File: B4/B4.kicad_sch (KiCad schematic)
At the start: 0 parts

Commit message: B0 ready for v0.2.0 release.
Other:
- sheet buses ports: added DZ[0..7], D[0..7], ~{EN[0..15]}; removed {DATABUS}, {ENABLEBUS}
- company: (none) -> Daniel Molina
- title: (none) -> 74HCT6526 Board 4
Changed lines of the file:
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@@
 (kicad_sch (version 20211123) (generator eeschema)
   (paper "A4")
+  (title_block
+    (title "74HCT6526 Board 4")
+    (date "2023-01-22")
+    (rev "0.2.0")
+    (company "Daniel Molina")
+    (comment 1 "https://github.com/dmolinagarcia/74HCT6526")
+  )
   (bus_alias "ENABLEBUS" (members "~{EN[0..15]}"))
   (bus_alias "DATABUS" (members "D[0..7]" "DZ[0..7]"))
@@
   (junction (at 43.18 17.78) (diameter 1.016) (color 0 0 0 0)
   )
-  (junction (at 48.26 22.86) (diameter 0.9144) (color 0 0 0 0)
+  (junction (at 48.26 25.4) (diameter 0) (color 0 0 0 0)
+  )
+  (junction (at 50.8 22.86) (diameter 0) (color 0 0 0 0)
   )
   (junction (at 45.72 20.32) (diameter 1.016) (color 0 0 0 0)
@@
     (stroke (width 0) (type solid) (color 0 0 0 0))
   )
+  (bus (pts (xy 48.26 50.8) (xy 48.26 25.4))
+    (stroke (width 0) (type default) (color 0 0 0 0))
+  )
   (bus (pts (xy 43.18 17.78) (xy 284.48 17.78))
     (stroke (width 0) (type solid) (color 0 0 0 0))
   )
-  (bus (pts (xy 40.64 50.8) (xy 48.26 50.8))
+  (bus (pts (xy 40.64 53.34) (xy 50.8 53.34))
     (stroke (width 0) (type solid) (color 0 0 0 0))
   )
@@
     (stroke (width 0) (type solid) (color 0 0 0 0))
   )
-  (bus (pts (xy 48.26 50.8) (xy 48.26 22.86))
+  (bus (pts (xy 50.8 53.34) (xy 50.8 22.86))
     (stroke (width 0) (type solid) (color 0 0 0 0))
   )
   (bus (pts (xy 40.64 45.72) (xy 43.18 45.72))
     (stroke (width 0) (type solid) (color 0 0 0 0))
+  )
+  (bus (pts (xy 48.26 25.4) (xy 284.48 25.4))
+    (stroke (width 0) (type default) (color 0 0 0 0))
+  )
+  (bus (pts (xy 40.64 25.4) (xy 48.26 25.4))
+    (stroke (width 0) (type default) (color 0 0 0 0))
+  )
+  (bus (pts (xy 40.64 50.8) (xy 48.26 50.8))
+    (stroke (width 0) (type default) (color 0 0 0 0))
   )
   (bus (pts (xy 43.18 17.78) (xy 43.18 45.72))
@@
     (stroke (width 0) (type solid) (color 0 0 0 0))
   )
-  (bus (pts (xy 40.64 22.86) (xy 48.26 22.86))
+  (bus (pts (xy 40.64 22.86) (xy 50.8 22.86))
     (stroke (width 0) (type solid) (color 0 0 0 0))
   )
-  (bus (pts (xy 48.26 22.86) (xy 284.48 22.86))
+  (bus (pts (xy 50.8 22.86) (xy 284.48 22.86))
     (stroke (width 0) (type solid) (color 0 0 0 0))
   )
@@
     (stroke (width 0) (type solid) (color 0 0 0 0))
   )
-  (label "{DATABUS}" (at 281.94 20.32 180)
-    (effects (font (size 1.27 1.27)) (justify right bottom))
-  )
-  (label "{ENABLEBUS}" (at 281.94 22.86 180)
-    (effects (font (size 1.27 1.27)) (justify right bottom))
-  )
   (label "{CONTROLBUS}" (at 281.94 17.78 180)
     (effects (font (size 1.27 1.27)) (justify right bottom))
   )
-  (global_label "{DATABUS}" (shape input) (at 40.64 20.32 180)
+  (global_label "D[0..7]" (shape input) (at 40.64 20.32 180)
     (effects (font (size 1.27 1.27)) (justify right))
     (property "Intersheet References" "${INTERSHEET_REFS}" (id 0) (at 26.7848 20.2406 0)
@@
     )
   )
-  (global_label "{ENABLEBUS}" (shape input) (at 40.64 22.86 180)
+  (global_label "~{EN[0..15]}" (shape input) (at 40.64 22.86 180)
     (effects (font (size 1.27 1.27)) (justify right))
     (property "Intersheet References" "${INTERSHEET_REFS}" (id 0) (at 24.1843 22.7806 0)
@@
     (effects (font (size 1.27 1.27)) (justify right))
     (property "Intersheet References" "${INTERSHEET_REFS}" (id 0) (at 22.6724 17.7006 0)
+      (effects (font (size 1.27 1.27)) (justify right) hide)
+    )
+  )
+  (global_label "DZ[0..7]" (shape input) (at 40.64 25.4 180)
+    (effects (font (size 1.27 1.27)) (justify right))
+    (property "Intersheet References" "${INTERSHEET_REFS}" (id 0) (at 26.7848 25.3206 0)
       (effects (font (size 1.27 1.27)) (justify right) hide)
     )
@@
       (effects (font (size 1.27 1.27)) (justify right))
     )
-    (pin "{DATABUS}" bidirectional (at 40.64 48.26 0)
+    (pin "D[0..7]" bidirectional (at 40.64 48.26 0)
       (effects (font (size 1.27 1.27)) (justify right))
     )
-    (pin "{ENABLEBUS}" input (at 40.64 50.8 0)
+    (pin "~{EN[0..15]}" input (at 40.64 53.34 0)
+      (effects (font (size 1.27 1.27)) (justify right))
+    )
+    (pin "DZ[0..7]" bidirectional (at 40.64 50.8 0)
       (effects (font (size 1.27 1.27)) (justify right))
     )
@@
       (reference "#PWR04") (unit 1) (value "GND") (footprint "")
     )
+    (path "/ab70af84-b545-4f99-8702-a579edb051a6/8554bcb8-444f-4ed6-8d2e-98ad945f68d5"
+      (reference "#PWR?") (unit 1) (value "GND") (footprint "")
+    )
+    (path "/ab70af84-b545-4f99-8702-a579edb051a6/989f85db-f560-481a-baba-d8c4193b2250"
+      (reference "C400") (unit 1) (value "100n") (footprint "")
+    )
     (path "/ab70af84-b545-4f99-8702-a579edb051a6/eb77a2b8-05ae-49a3-b81c-407677587e70"

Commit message: Ready for v0.2.1
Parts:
- added U401, U402: 74HC00, symbol 74xx:74HC00
- added U403: 74HC04, Package_SO:SOIC-14_3.9x8.7mm_P1.27mm, symbol 74xx:74HC04
- added U404, U405, U406: 74HC32, symbol 74xx:74LS32
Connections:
- new net PHI2: U403.1
- new net ~{PHI2}: U403.2
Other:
- added sheet todAlarm (todAlarm.kicad_sch)
- added sheet todComparator (todComparator.kicad_sch)
- added sheet todControl (todControl.kicad_sch)
- added sheet todCounter (todCounter.kicad_sch)
- added sheet todOutput (todOutput.kicad_sch)

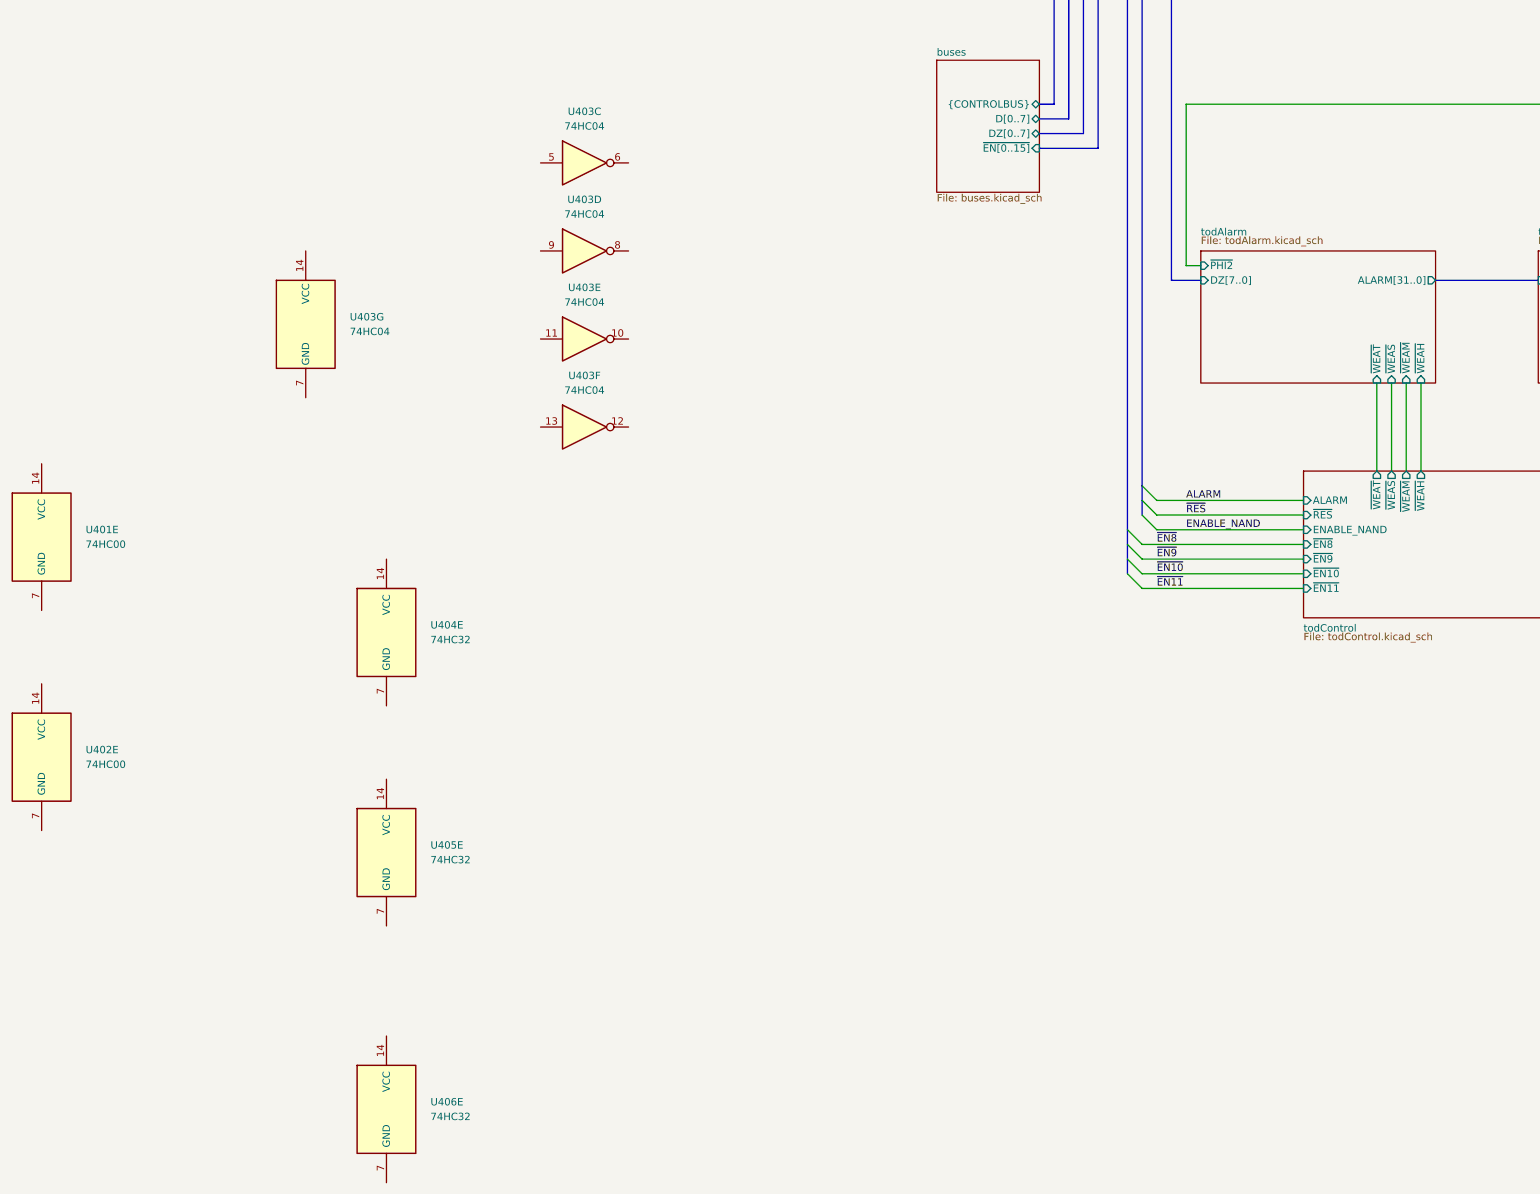
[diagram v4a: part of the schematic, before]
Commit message: B2 refactored. B4 Added. TOD sch completed.
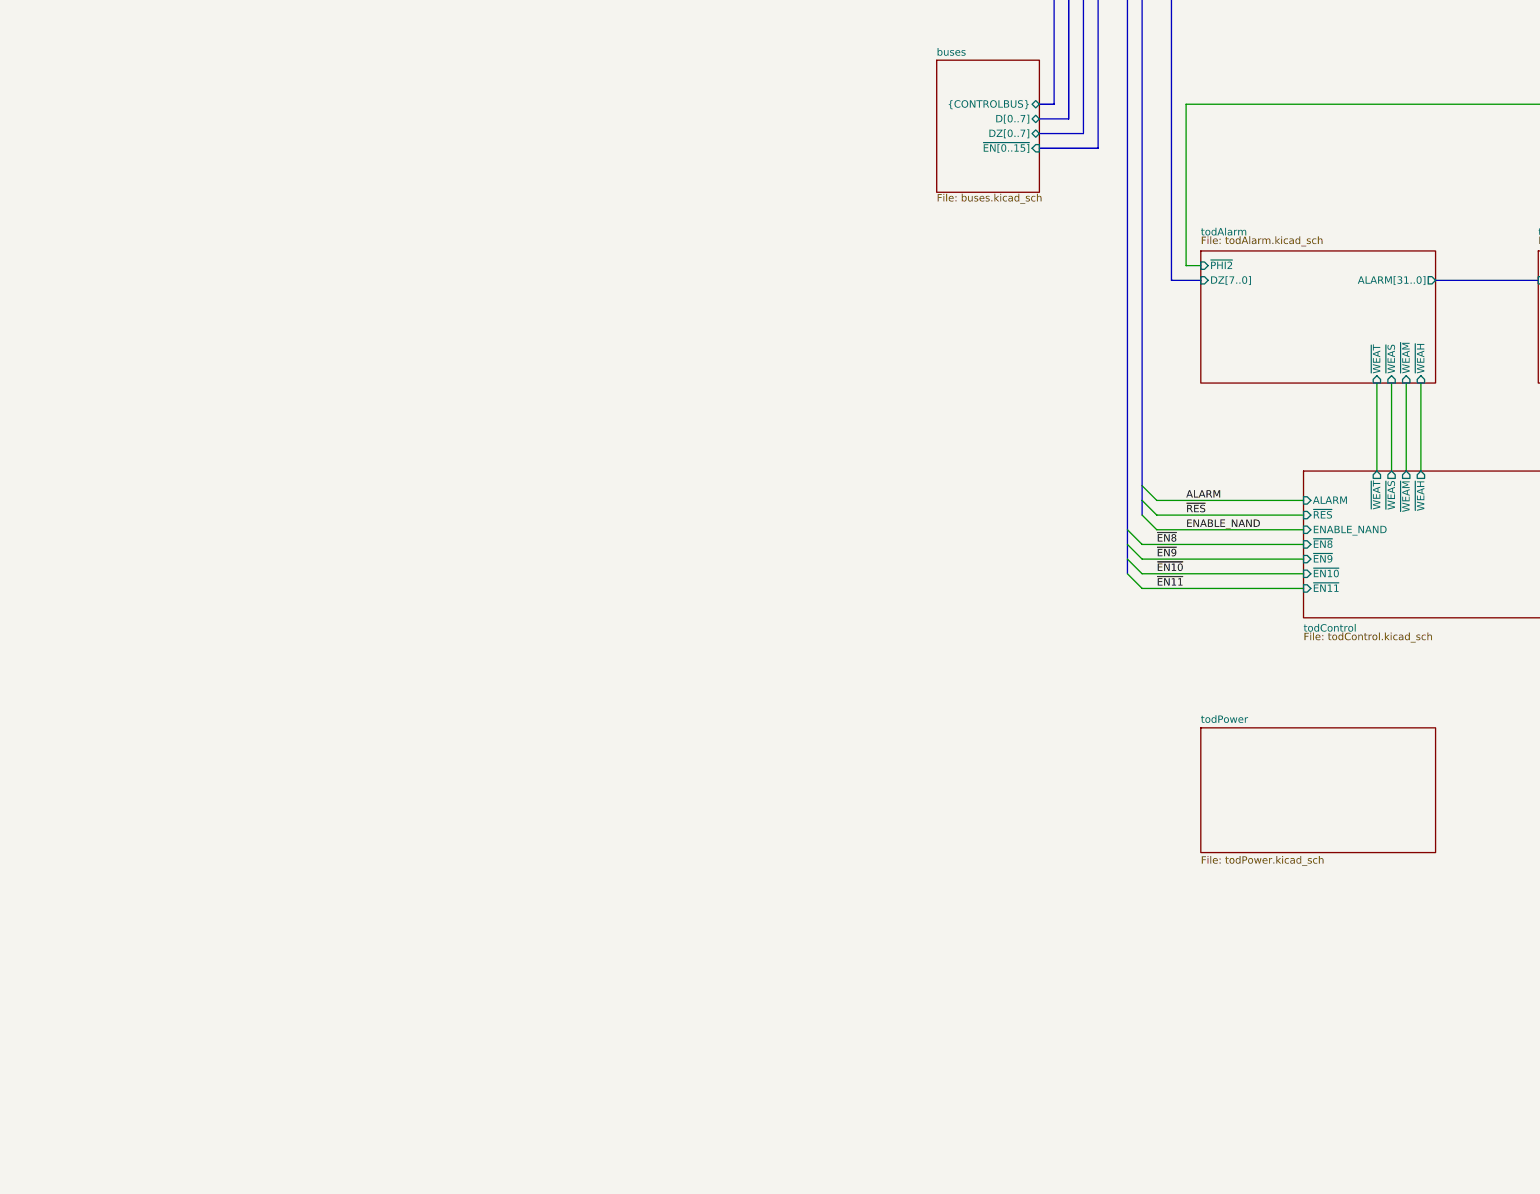
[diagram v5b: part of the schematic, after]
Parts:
- removed U401, U402: 74HC00, symbol 74xx:74HC00
- removed unit 5 of U403
- removed unit 7 of U403
- removed unit 4 of U403
- removed unit 3 of U403
- removed unit 6 of U403
- removed U404, U405, U406: 74HC32, symbol 74xx:74LS32
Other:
- added sheet todPower (todPower.kicad_sch)

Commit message: TOD is here
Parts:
- renumbered U403 to U503
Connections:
- net PHI2: now also U503.9; no longer U503.1
- net ~{PHI2}: now also U503.8; no longer U503.2

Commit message: Ready for v0.2.2
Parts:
- renumbered U503 to U429
